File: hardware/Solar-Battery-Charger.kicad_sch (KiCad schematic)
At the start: 48 parts, among them J3 Conn_01x02_Female, J4 Tab_Amp_1217861-1, J5 Tab_Amp_1217861-1, J6 Tab_Amp_1217861-1, J7 Tab_Amp_1217861-1, Q1 AO4882, Q2 2N7002, U2 LM234Z-3, U3 NSL-32, U4 BQ24650RVAT, U5 NSL-32

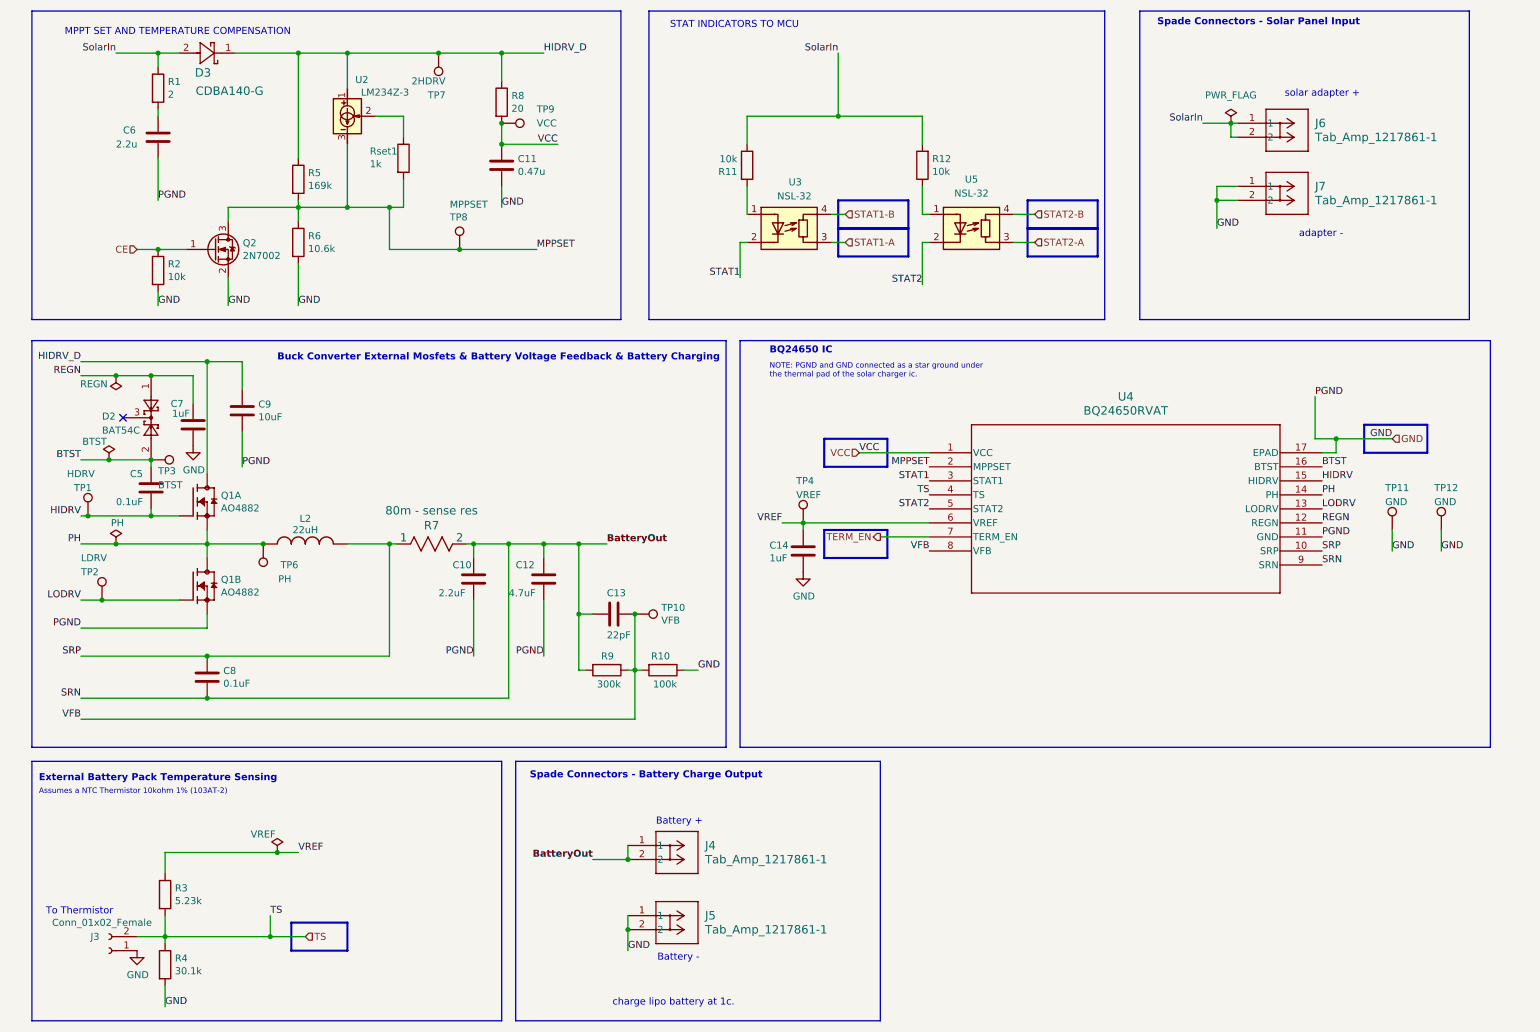
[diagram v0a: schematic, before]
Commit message: feat(hw): redesign charger stage from the BQ24650 reference design
Rebuild the charger sheet against the BQ24650 datasheet and the
BQ24650EVM-639 reference design: PDS1040-13 and ZLLS350TA Schottky
diodes, SI7288DP-T1-GE3 dual MOSFET, input and output filtering, and
test points per the EVM. Every symbol now resolves from
KiCad-Master-Lib; the *-rescue, kml-custom and SparkFun references are
gone, and the top sheet drops the unused I2C header.

The bootstrap diode is oriented REGN -> BTST as the datasheet requires,
and the BQ24650 VCC net carries a PWR_FLAG since it is fed through the
input filter resistors. ERC is clean at all severities.

The PCB is cleared for re-layout: the Nano socket, buck stage and
mechanicals are placed, nothing is routed, and DRC schematic parity
reports 66 missing footprints until layout lands.
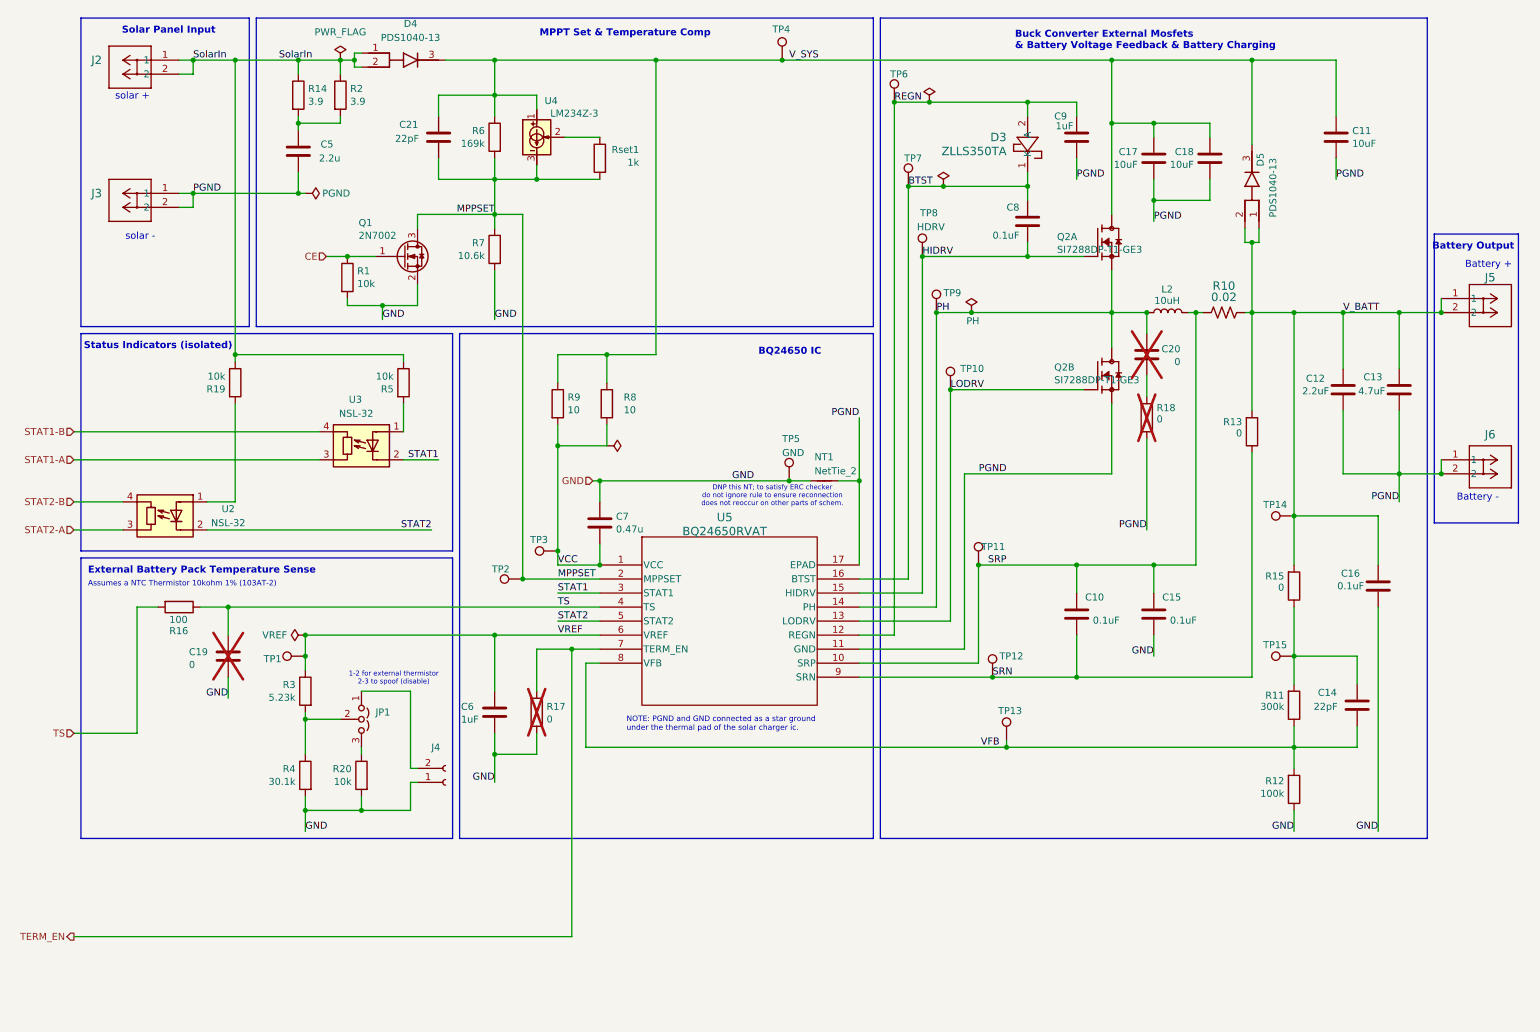
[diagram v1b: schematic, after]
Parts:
- removed C10: 2.2uF, Capacitor_SMD:C_0805_2012Metric, symbol Device:C
- removed C11: 0.47u, Capacitor_SMD:C_0805_2012Metric, symbol Device:C
- removed D2: BAT54C, Package_TO_SOT_SMD:SOT-23, symbol Diode:BAT54C
- removed D3: CDBA140-G, KMLib_Passives_SMD:CDBA-G, symbol kml-custom:CDBA140-G
- removed J3: Conn_01x02_Female, TerminalBlock_Phoenix:TerminalBlock_Phoenix_MPT-0,5-2-2.54_1x02_P2.54mm_Horizontal, symbol Solar-Battery-Charger-rescue:Conn_01x02_Female-Connector
- removed L2: 22uH, Inductor_SMD:L_0805_2012Metric, symbol Solar-Battery-Charger-rescue:CBC3225T100MRV-CBC3225T100MRV
- removed R12: 10k, Resistor_SMD:R_0805_2012Metric, symbol Device:R
- removed TP10: VFB, TestPoint:TestPoint_Loop_D1.80mm_Drill1.0mm_Beaded, symbol Connector:TestPoint
- removed TP4: VREF, TestPoint:TestPoint_Loop_D1.80mm_Drill1.0mm_Beaded, symbol Connector:TestPoint
- removed TP9: VCC, TestPoint:TestPoint_Loop_D1.80mm_Drill1.0mm_Beaded, symbol Connector:TestPoint
- removed U5: NSL-32, OptoDevice:Luna_NSL-32, symbol Isolator:NSL-32
- added C14, C21: 22pF, Capacitor_SMD:C_0805_2012Metric, symbol Device:C
- added C15, C16: 0.1uF, Capacitor_SMD:C_0805_2012Metric, symbol Device:C
- added C17, C18: 10uF, Capacitor_SMD:C_0805_2012Metric, symbol Device:C
- added C19, C20: 0, Capacitor_SMD:C_0805_2012Metric, symbol Device:C
- added C7: 0.47u, Capacitor_SMD:C_0805_2012Metric, symbol Device:C
- added D3: ZLLS350TA, KMLib_IC_SMD:DIODE_SOD-523_DIO, symbol KMLib_Discrete_Semiconductors:ZLLS350TA
- added D4, D5: PDS1040-13, KMLib_IC_SMD:POWERDI5_DIO, symbol KMLib_Discrete_Semiconductors:PDS1040-13
- added J4: Conn_01x02_Female, TerminalBlock_TE-Connectivity:TerminalBlock_TE_282834-2_1x02_P2.54mm_Horizontal, symbol Connector:Conn_01x02_Socket
- added JP1: Jumper_3_Open, symbol Jumper:Jumper_3_Open
- added L2: 10uH, Inductor_SMD:L_0805_2012Metric, symbol Device:L
- added NT1: NetTie_2, symbol Device:NetTie_2
- added R13, R15, R17, R18: 0, Resistor_SMD:R_0805_2012Metric, symbol Device:R
- added R14: 3.9, Resistor_SMD:R_0805_2012Metric, symbol Device:R
- added R16: 100, Resistor_SMD:R_0805_2012Metric, symbol Device:R
- added R19, R20: 10k, Resistor_SMD:R_0805_2012Metric, symbol Device:R
- added R9: 10, Resistor_SMD:R_0805_2012Metric, symbol Device:R
- added TP1: VREF, TestPoint:TestPoint_Loop_D1.80mm_Drill1.0mm_Beaded, symbol Connector:TestPoint
- added TP13: VFB, TestPoint:TestPoint_Loop_D1.80mm_Drill1.0mm_Beaded, symbol Connector:TestPoint
- added TP14, TP15: SRP, TestPoint:TestPoint_Loop_D1.80mm_Drill1.0mm_Beaded, symbol Connector:TestPoint
- added TP5: GND, TestPoint:TestPoint_Loop_D1.80mm_Drill1.0mm_Beaded, symbol Connector:TestPoint
- added TP6: REGN, TestPoint:TestPoint_Loop_D1.80mm_Drill1.0mm_Beaded, symbol Connector:TestPoint
- added TP7: BTST, TestPoint:TestPoint_Loop_D1.80mm_Drill1.0mm_Beaded, symbol Connector:TestPoint
- added U2: NSL-32, OptoDevice:Luna_NSL-32, symbol Isolator:NSL-32
- C12: value 4.7uF -> 2.2uF
- C13: value 22pF -> 4.7uF
- J2: renamed from J6; footprint KML-Custom:CONN_1217861-1_TEC -> KMLib_Connectors:1217861-1_Tab; symbol kml-custom:Tab_Amp_1217861-1 -> KMLib_Connectors:1217861-1_Tab
- J3: renamed from J7; footprint KML-Custom:CONN_1217861-1_TEC -> KMLib_Connectors:1217861-1_Tab; symbol kml-custom:Tab_Amp_1217861-1 -> KMLib_Connectors:1217861-1_Tab
- J5: renamed from J4; footprint KML-Custom:CONN_1217861-1_TEC -> KMLib_Connectors:1217861-1_Tab; symbol kml-custom:Tab_Amp_1217861-1 -> KMLib_Connectors:1217861-1_Tab
- J6: renamed from J5; footprint KML-Custom:CONN_1217861-1_TEC -> KMLib_Connectors:1217861-1_Tab; symbol kml-custom:Tab_Amp_1217861-1 -> KMLib_Connectors:1217861-1_Tab
- Q2: renamed from Q1; value AO4882 -> SI7288DP-T1-GE3; footprint Package_SO:SOIC-8_3.9x4.9mm_P1.27mm -> KMLib_IC_SMD:POWERPAK_SO-8_DUAL_VIS; symbol Solar-Battery-Charger-rescue:SI7288DP-T1-GE3-SI7288DP-T1-GE3 -> KMLib_Discrete_Semiconductors:SI7288DP-T1-GE3
- R10: renamed from R7; value 80m - sense res -> 0.02; symbol Solar-Battery-Charger-rescue:WSLP1206R0200FEA-2020-04-21_06-00-44 -> Device:R_US; Note (none) -> WSLP1206R0200FEA
- R2: renamed from R1; value 2 -> 3.9
- R8: value 20 -> 10
- TP11: value GND -> SRP
- TP12: value GND -> SRN
- TP3: value BTST -> VCC
- TP4: renamed from TP7; value 2HDRV -> V_SYS
- renumbered C8 to C10, C9 to C11, C6 to C5, C14 to C6, C5 to C8, C7 to C9, Q2 to Q1, R2 to R1, R9 to R11, R10 to R12, R11 to R5, R5 to R6, R6 to R7, TP2 to TP10, TP8 to TP2, TP1 to TP8, TP6 to TP9, U2 to U4, U4 to U5
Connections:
- net BTST: now also D3.1 (K), TP7.1; no longer TP3.1
- net GND: now also C15.1, C16.1, C19.2, C7.1, J4.1 (Pin_1), NT1.2, R17.1, R20.2, TP5.1; no longer C11.2, C12.1, C5.2, C9.2, J3.1, J3.2, J6.1, J6.2, Q2.1 (S2), TP11.1, TP12.1, U5.11 (GND), U5.17 (EPAD)
- net HIDRV: now also Q2.2 (G1); no longer Q2.4 (G1)
- net LODRV: now also Q2.4 (G2); no longer Q2.2 (G2)
- net MPPSET: now also C21.2
- net PH: now also Q2.1 (S1), Q2.5 (D2), Q2.6 (D2), C20.1, L2.1; no longer Q2.3 (S1), Q2.7 (D2), Q2.8 (D2)
- net REGN: now also D3.2 (A), TP6.1
- net SRP: now also TP11.1, C15.2, L2.2
- net STAT2: now also U2.2 (K)
- net STAT2-A: now also U2.3 (R)
- net STAT2-B: now also U2.4 (R)
- net SolarIn: now also D4.1 (A1), D4.2 (A2), R14.1, R19.1
- net TERM_EN: now also R17.2
- net TS: now also C19.1, R16.1, R16.2; no longer R3.2, R4.1
- net VCC: now also TP3.1, C7.2, R9.2
- net VFB: now also C14.2, TP13.1; no longer C13.2
- net VREF: now also TP1.1
- net at C5.1, R2.2: now also R14.2
- net BatteryOut renamed V_BATT
- net V_BATT: now also C13.2, C16.2, D5.1 (A1), D5.2 (A2), R13.2, R15.2, TP14.1; no longer C10.1, C13.1, R11.2, U5.9 (SRN)
- net HIDRV_D renamed V_SYS
- net V_SYS: now also Q2.7 (D1), Q2.8 (D1), C17.1, C18.1, C21.1, D4.3 (K), D5.3 (K), R9.1; no longer Q2.5 (D1), Q2.6 (D1)
- new net: JP1.2 (C), R3.2, R4.1
- new net: C14.1, R11.2, R15.1, TP15.1
- new net: R19.2, U2.1 (A)
- new net: C20.2, R18.2
- new net: JP1.3 (B), R20.1
- new net: J4.2 (Pin_2), JP1.1 (A)
- new net PGND: C11.2, C12.1, C13.1, C17.2, C18.2, C5.2, C9.2, J3.1, J3.2, J6.1, J6.2, NT1.1, Q2.3 (S2), R18.1, U5.11 (GND), U5.17 (EPAD)
- new net SRN: C10.1, R13.1, TP12.1, U5.9 (SRN)
- no-connect marks 1 -> 0
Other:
- note added: "1-2 for external thermistor 2-3 to spoof (disable)"
- note added: "Battery Output"
- note added: "DNP this NT; to satisfy ERC checker do not ignore rule to ensure reconnection does not reoccur on other parts of schem."
- note added: "External Battery Pack Temperature Sense"
- note added: "MPPT Set & Temperature Comp"
- note added: "Solar Panel Input"
- note added: "Status Indicators (isolated)"
- note added: "solar +"
- note added: "solar -"
- note removed: "External Battery Pack Temperature Sensing"
- note removed: "MPPT SET AND TEMPERATURE COMPENSATION"
- note removed: "STAT INDICATORS TO MCU"
- note removed: "Spade Connectors - Battery Charge Output"
- note removed: "Spade Connectors - Solar Panel Input"
- note removed: "To Thermistor"
- note removed: "adapter -"
- note removed: "charge lipo battery at 1c."
- note removed: "solar adapter +"
- moved on the sheet: C10, C11, C5, C6, C8, C9, J2, J3, J5, J6, Q1, Q2A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
